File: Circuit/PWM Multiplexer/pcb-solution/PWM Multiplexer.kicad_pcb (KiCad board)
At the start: 2 copper layers, 71 parts, among them J1 JST connector, Q1 S8050, Q10 S8050, Q11 S8050, Q12 S8050, Q13 S8050, Q14 S8050, Q2 S8050, Q3 S8050, Q4 S8050, Q5 S8050, Q6 S8050, Q7 S8050, Q8 S8050, Q9 S8050, U1 74HC137, U2 74HC137, U3 L7805, U4 PC817, U5 PC817, U6 PC817, U7 PC817

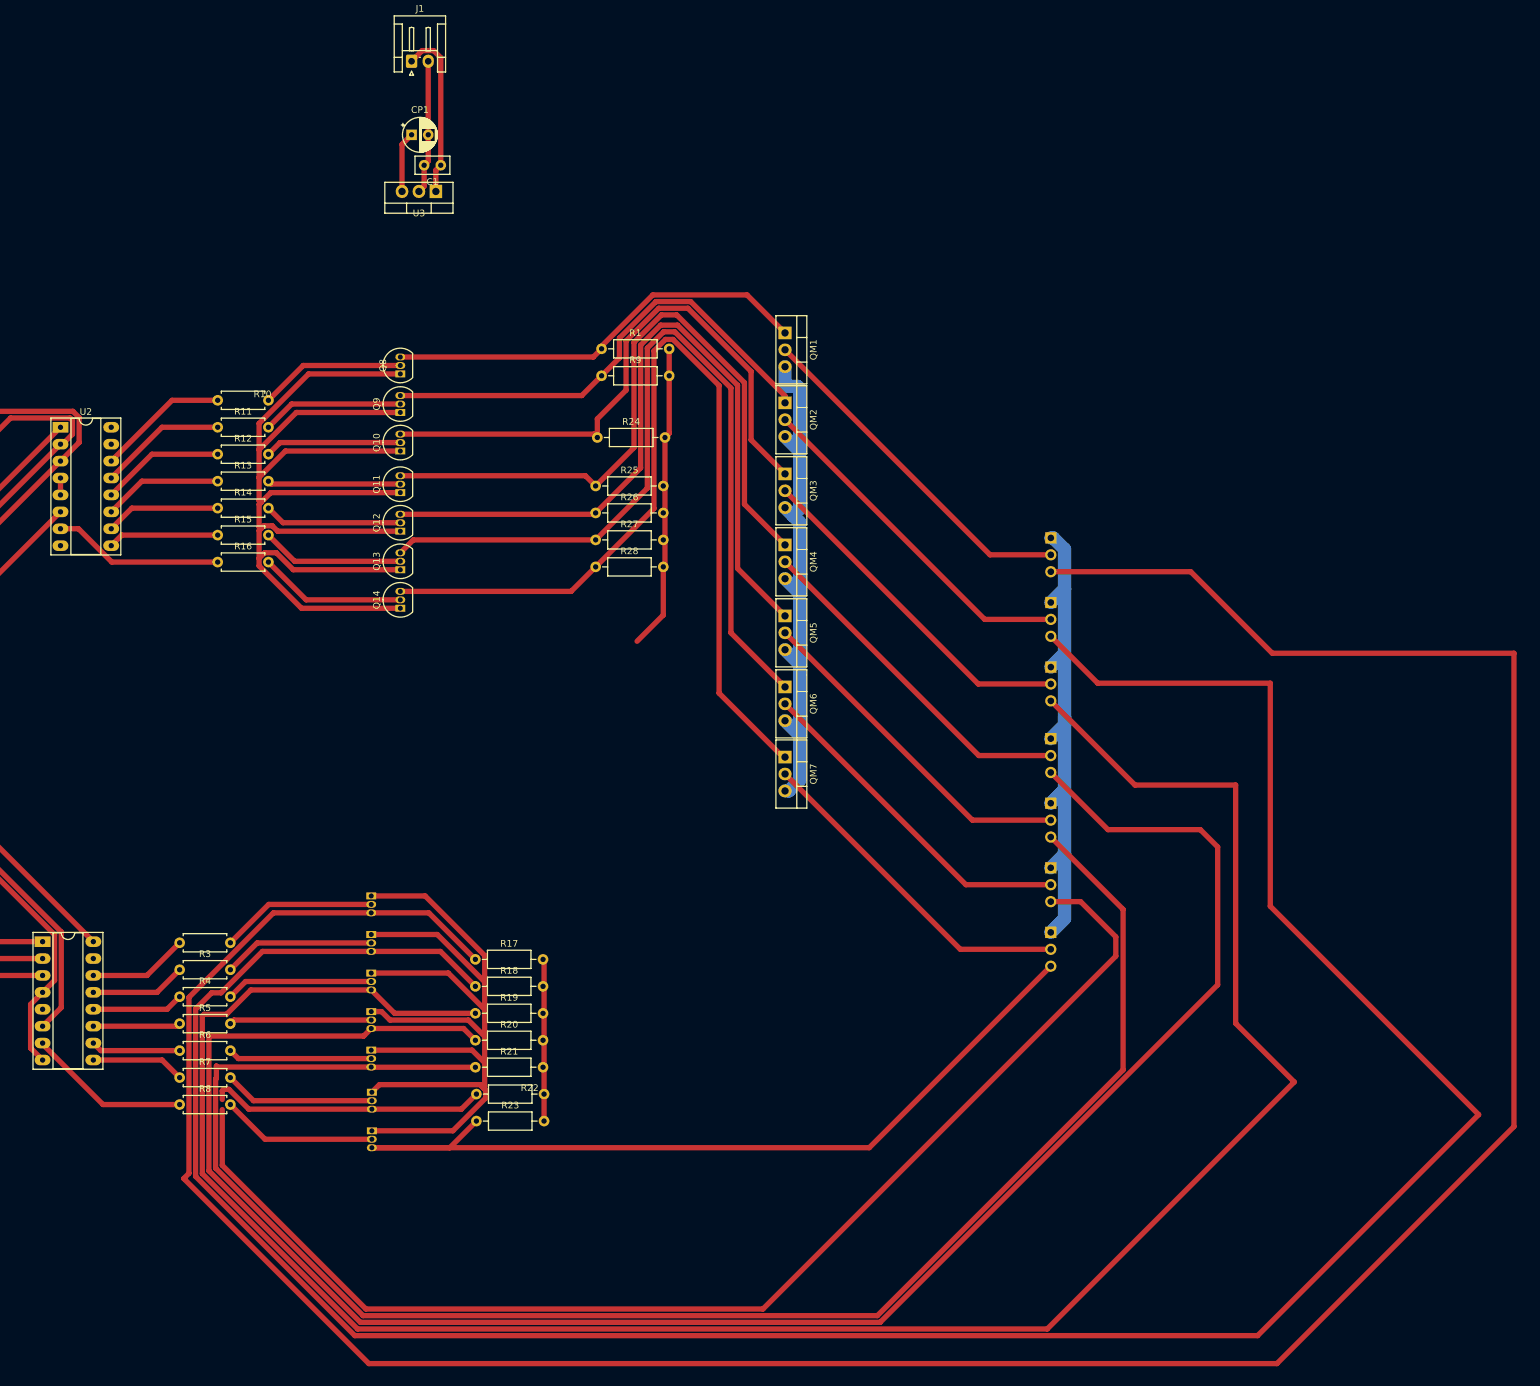
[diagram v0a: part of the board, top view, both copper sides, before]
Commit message: finished PWM multiplexer circuit final version
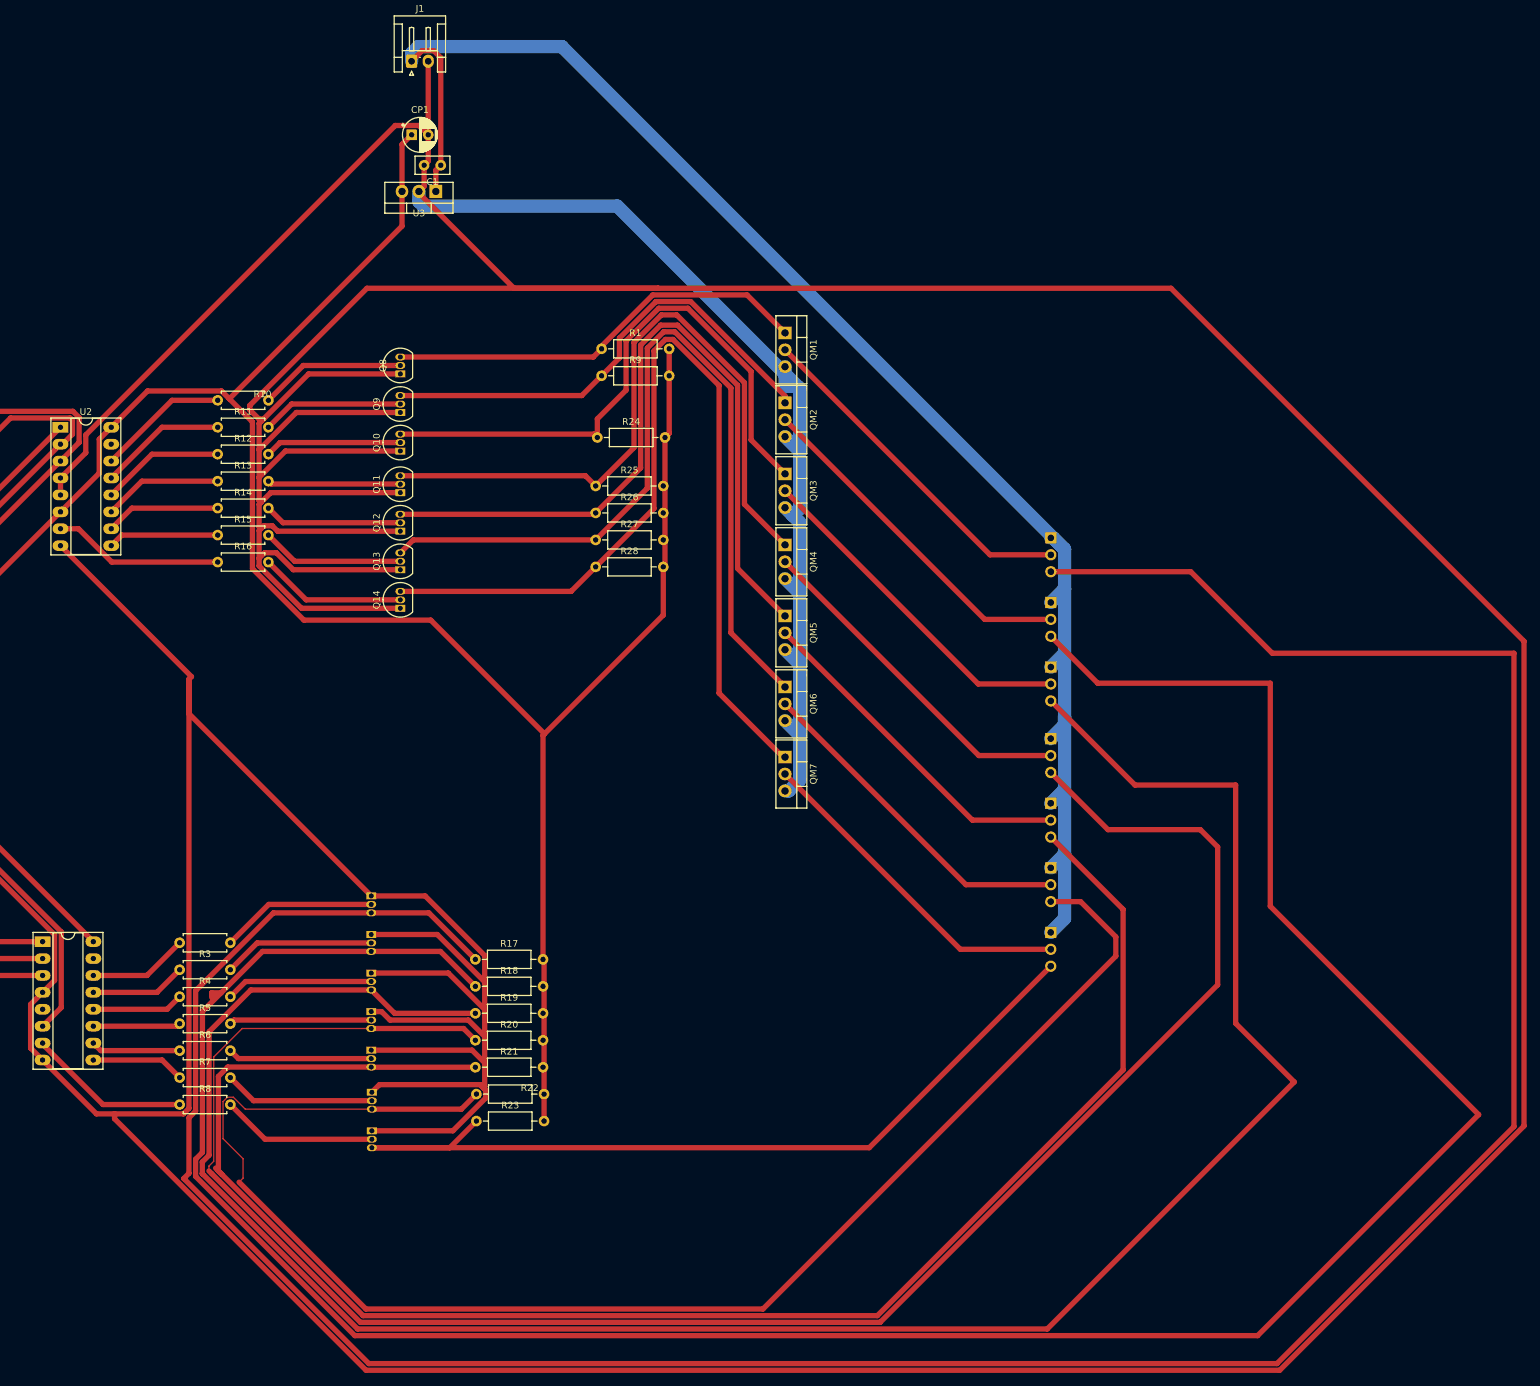
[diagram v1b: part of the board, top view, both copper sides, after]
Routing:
- net GND: track 545.5 -> 1439.7 mm
- net +5V: track 197.5 -> 410.5 mm
- net +12V: track 102.9 -> 233.9 mm
- net D4_PWM: track 293.8 -> 291.8 mm
- net D3_PWM: track 338.1 -> 336.2 mm
- net D2_PWM: track 403.0 -> 404.2 mm
